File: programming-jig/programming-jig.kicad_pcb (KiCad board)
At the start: 2 copper layers, 52 x 29 mm, 9 parts, among them J1 854-22-005-10-001101, J2 854-22-005-10-001101, J3 825-22-002-10-001101, J4 CONN_02X05, J5 USB_C_Receptacle

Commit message: Use power symbols in programming jig schematic
The power lines had been drawn as regular wires with net labels.  That's
not great, so I changed them to use power symbols.  It's better now!
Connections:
- net /GND renamed GND
- net /VBUS renamed VBUS
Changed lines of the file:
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@@
   (net 23 "Net-(J5-PadA8)")
   (net 24 "Net-(J5-PadA11)")
-  (net 25 /VBUS)
-  (net 26 /GND)
-  (net 27 "Net-(J5-PadB6)")
-  (net 28 "Net-(J5-PadB7)")
+  (net 25 "Net-(J5-PadB6)")
+  (net 26 "Net-(J5-PadB7)")
+  (net 27 VBUS)
+  (net 28 GND)
   (net_class Default "This is the default net class."
     (clearance 0.2)
@@
     (uvia_dia 0.3)
     (uvia_drill 0.1)
-    (add_net /GND)
-    (add_net /VBUS)
+    (add_net GND)
     (add_net "Net-(J1-Pad1)")
     (add_net "Net-(J1-Pad2)")
@@
     (add_net "Net-(J5-PadB7)")
     (add_net "Net-(J5-PadB8)")
+    (add_net VBUS)
   )
   (module pd-buddy:Pogo_Pin_Straight_1x05_Pitch1.27mm (layer F.Cu)
@@
     (fp_line (start -4.59 9.59) (end -4.59 -0.91) (layer F.Fab) (width 0.12))
     (pad B6 thru_hole circle (at 0.4 0.65 270) (size 0.65 0.65) (drill 0.4) (layers *.Cu *.Mask)
-      (net 27 "Net-(J5-PadB6)"))
+      (net 25 "Net-(J5-PadB6)"))
     (pad B7 thru_hole circle (at -0.4 0.65 270) (size 0.65 0.65) (drill 0.4) (layers *.Cu *.Mask)
-      (net 28 "Net-(J5-PadB7)"))
+      (net 26 "Net-(J5-PadB7)"))
     (pad S1 thru_hole circle (at -4.13 1.25 270) (size 1.4 1.4) (drill 1.1) (layers *.Cu *.Mask)
-      (net 26 /GND))
+      (net 28 GND))
     (pad B9 thru_hole circle (at -1.2 0.65 270) (size 0.65 0.65) (drill 0.4) (layers *.Cu *.Mask)
-      (net 25 /VBUS))
+      (net 27 VBUS))
     (pad B4 thru_hole circle (at 1.2 0.65 270) (size 0.65 0.65) (drill 0.4) (layers *.Cu *.Mask)
-      (net 25 /VBUS))
+      (net 27 VBUS))
     (pad B12 thru_hole circle (at -2.8 0.65 270) (size 0.65 0.65) (drill 0.4) (layers *.Cu *.Mask)
-      (net 26 /GND))
+      (net 28 GND))
     (pad B5 thru_hole circle (at 0.8 1.35 270) (size 0.65 0.65) (drill 0.4) (layers *.Cu *.Mask)
       (net 13 "Net-(J5-PadB5)"))
@@
       (net 18 "Net-(J5-PadB11)"))
     (pad A1 smd rect (at -2.75 -0.66 270) (size 0.3 0.7) (layers F.Cu F.Paste F.Mask)
-      (net 26 /GND))
+      (net 28 GND))
     (pad A2 smd rect (at -2.25 -0.66 270) (size 0.3 0.7) (layers F.Cu F.Paste F.Mask)
       (net 19 "Net-(J5-PadA2)"))
@@
       (net 20 "Net-(J5-PadA3)"))
     (pad A4 smd rect (at -1.25 -0.66 270) (size 0.3 0.7) (layers F.Cu F.Paste F.Mask)
-      (net 25 /VBUS))
+      (net 27 VBUS))
     (pad A5 smd rect (at -0.75 -0.66 270) (size 0.3 0.7) (layers F.Cu F.Paste F.Mask)
       (net 21 "Net-(J5-PadA5)"))
@@
       (net 12 "Net-(J5-PadA7)"))
     (pad A12 smd rect (at 2.75 -0.66 270) (size 0.3 0.7) (layers F.Cu F.Paste F.Mask)
-      (net 26 /GND))
+      (net 28 GND))
     (pad A10 smd rect (at 1.75 -0.66 270) (size 0.3 0.7) (layers F.Cu F.Paste F.Mask)
       (net 22 "Net-(J5-PadA10)"))
     (pad A9 smd rect (at 1.25 -0.66 270) (size 0.3 0.7) (layers F.Cu F.Paste F.Mask)
-      (net 25 /VBUS))
+      (net 27 VBUS))
     (pad A8 smd rect (at 0.75 -0.66 270) (size 0.3 0.7) (layers F.Cu F.Paste F.Mask)
       (net 23 "Net-(J5-PadA8)"))
@@
       (net 24 "Net-(J5-PadA11)"))
     (pad B1 thru_hole circle (at 2.8 0.65 270) (size 0.65 0.65) (drill 0.4) (layers *.Cu *.Mask)
-      (net 26 /GND))
+      (net 28 GND))
     (pad S1 thru_hole circle (at 4.13 1.25 270) (size 1.4 1.4) (drill 1.1) (layers *.Cu *.Mask)
-      (net 26 /GND))
+      (net 28 GND))
     (pad S1 thru_hole circle (at 4.49 7.2 270) (size 1.4 1.4) (drill 1.1) (layers *.Cu *.Mask)
-      (net 26 /GND))
+      (net 28 GND))
     (pad S1 thru_hole circle (at -4.49 7.2 270) (size 1.4 1.4) (drill 1.1) (layers *.Cu *.Mask)
-      (net 26 /GND))
+      (net 28 GND))
     (pad "" np_thru_hole circle (at 3.6 0 270) (size 0.95 0.95) (drill 0.95) (layers *.Cu *.Mask))
     (pad "" np_thru_hole circle (at -3.6 0 270) (size 0.65 0.65) (drill 0.65) (layers *.Cu *.Mask))
@@
       (net 13 "Net-(J5-PadB5)"))
     (pad 2 smd rect (at 0.95 0 90) (size 0.7 1.3) (layers F.Cu F.Paste F.Mask)
-      (net 26 /GND))
+      (net 28 GND))
     (model ${KISYS3DMOD}/Resistors_SMD.3dshapes/R_0805.wrl
       (at (xyz 0 0 0))
@@
       (net 21 "Net-(J5-PadA5)"))
     (pad 2 smd rect (at 0.95 0 90) (size 0.7 1.3) (layers F.Cu F.Paste F.Mask)
-      (net 26 /GND))
+      (net 28 GND))
     (model ${KISYS3DMOD}/Resistors_SMD.3dshapes/R_0805.wrl
       (at (xyz 0 0 0))
@@
     )
     (pad 1 thru_hole rect (at 0 0 90) (size 1.7 1.7) (drill 0.762) (layers *.Cu *.Mask)
-      (net 25 /VBUS))
+      (net 27 VBUS))
     (pad 2 thru_hole oval (at 0 2.54 90) (size 1.7 1.7) (drill 0.762) (layers *.Cu *.Mask)
-      (net 26 /GND))
+      (net 28 GND))
     (model ${KISYS3DMOD}/Pin_Headers.3dshapes/Pin_Header_Straight_1x02_Pitch2.54mm.wrl
       (at (xyz 0 -0.05 0))
@@
   (segment (start 94.25 112.5) (end 94.25 111.7) (width 0.25) (layer F.Cu) (net 21))
   (via (at 94.25 112.5) (size 0.6) (drill 0.4) (layers F.Cu B.Cu) (net 21))
-  (segment (start 92.25 109.8) (end 92.25 109) (width 0.25) (layer F.Cu) (net 26))
-  (via (at 92.25 109) (size 0.6) (drill 0.4) (layers F.Cu B.Cu) (net 26))
-  (segment (start 94.25 109.8) (end 94.25 109) (width 0.25) (layer F.Cu) (net 26))
-  (via (at 94.25 109) (size 0.6) (drill 0.4) (layers F.Cu B.Cu) (net 26))
-  (segment (start 96.91 122.5) (end 95.65 122.5) (width 0.25) (layer F.Cu) (net 26))
-  (segment (start 95.65 122.5) (end 95.6 122.55) (width 0.25) (layer F.Cu) (net 26))
-  (segment (start 96.91 117) (end 95.65 117) (width 0.25) (layer F.Cu) (net 26))
-  (segment (start 95.65 117) (end 95.6 116.95) (width 0.25) (layer F.Cu) (net 26))
-  (zone (net 26) (net_name /GND) (layer B.Cu) (hatch edge 0.508)
+  (segment (start 92.25 109.8) (end 92.25 109) (width 0.25) (layer F.Cu) (net 28))
+  (via (at 92.25 109) (size 0.6) (drill 0.4) (layers F.Cu B.Cu) (net 28))
+  (segment (start 94.25 109.8) (end 94.25 109) (width 0.25) (layer F.Cu) (net 28))
+  (via (at 94.25 109) (size 0.6) (drill 0.4) (layers F.Cu B.Cu) (net 28))
+  (segment (start 96.91 122.5) (end 95.65 122.5) (width 0.25) (layer F.Cu) (net 28))
+  (segment (start 95.65 122.5) (end 95.6 122.55) (width 0.25) (layer F.Cu) (net 28))
+  (segment (start 96.91 117) (end 95.65 117) (width 0.25) (layer F.Cu) (net 28))
+  (segment (start 95.65 117) (end 95.6 116.95) (width 0.25) (layer F.Cu) (net 28))
+  (zone (net 28) (net_name GND) (layer B.Cu) (hatch edge 0.508)
     (priority 1)
     (connect_pads (clearance 0.2))
@@
     )
   )
-  (zone (net 25) (net_name /VBUS) (layer F.Cu) (hatch edge 0.508)
+  (zone (net 27) (net_name VBUS) (layer F.Cu) (hatch edge 0.508)
     (priority 1)
     (connect_pads yes (clearance 0.2))

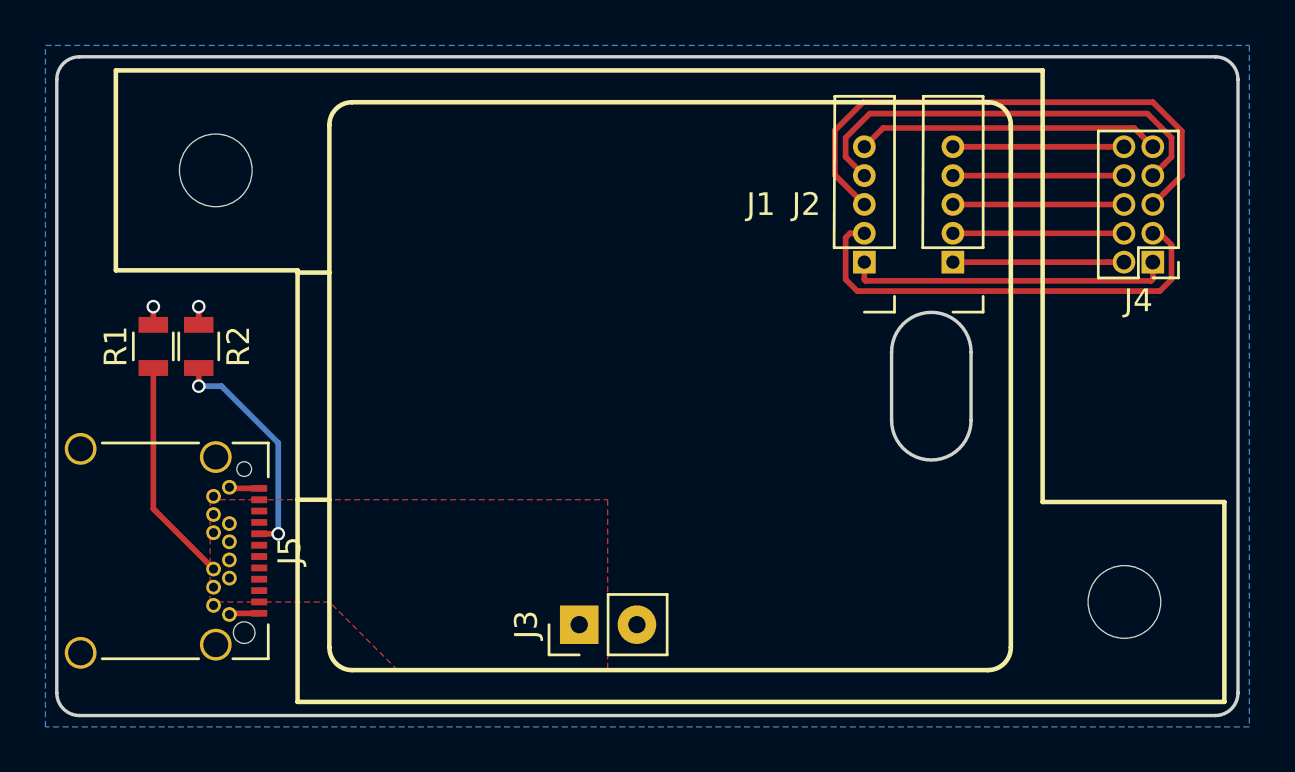
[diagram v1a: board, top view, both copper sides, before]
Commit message: Shrunk programming jig outline
By removing clearance around the printed piece, I was able to shrink the
board to 95.6% of the area it had before.  That'll save me a few cents.
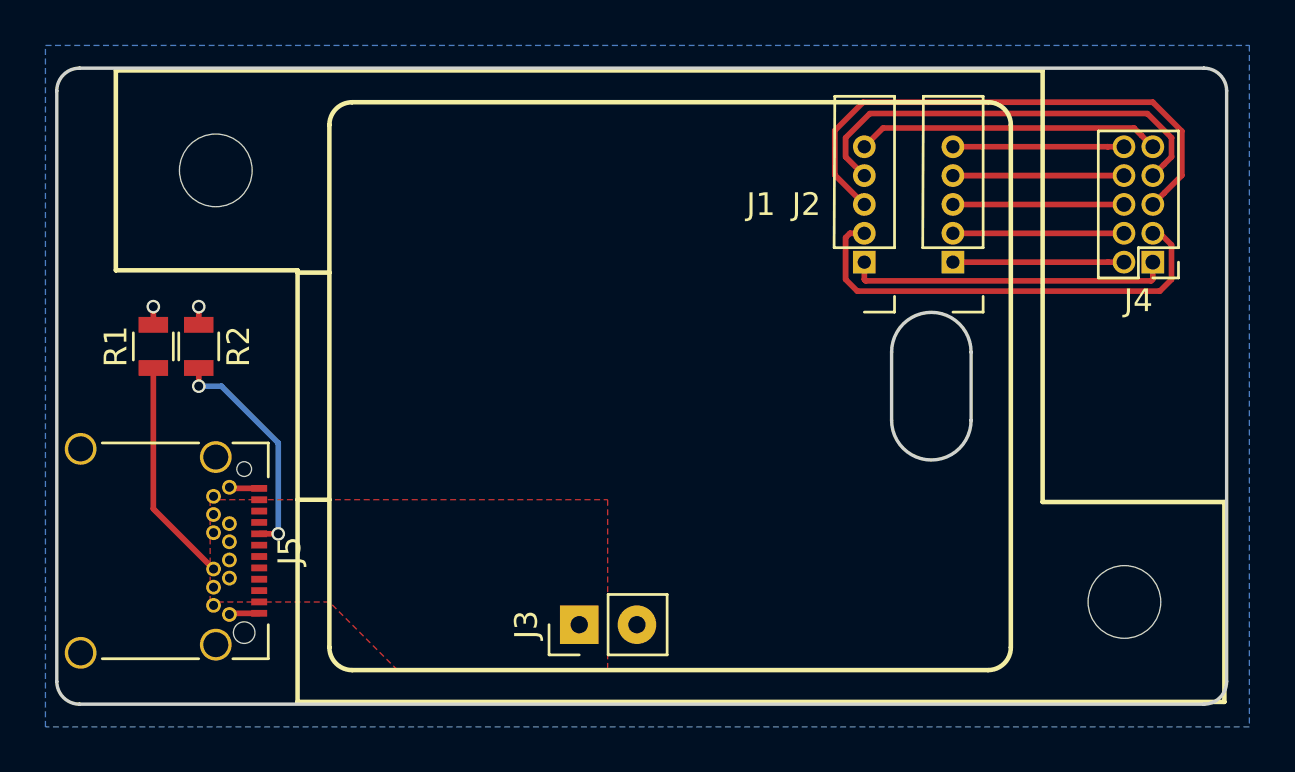
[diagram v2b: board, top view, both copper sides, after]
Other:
- board size 52 x 29 mm -> 51.5 x 28 mm
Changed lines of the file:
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@@
     (links 26)
     (no_connects 0)
-    (area 84.775 97.065 140.648334 133.295238)
+    (area 87.924999 98.424999 139.575001 126.575001)
     (thickness 1.6)
     (drawings 31)
@@
   (gr_arc (start 129 124) (end 130 124) (angle 90) (layer F.SilkS) (width 0.2))
   (gr_arc (start 129 101) (end 129 100) (angle 90) (layer F.SilkS) (width 0.2))
-  (gr_arc (start 139 99) (end 139 98) (angle 90) (layer Edge.Cuts) (width 0.15))
-  (gr_arc (start 89 99) (end 88 99) (angle 90) (layer Edge.Cuts) (width 0.15))
-  (gr_arc (start 89 126) (end 89 127) (angle 90) (layer Edge.Cuts) (width 0.15))
-  (gr_arc (start 139 126) (end 140 126) (angle 90) (layer Edge.Cuts) (width 0.15))
+  (gr_arc (start 138.5 99.5) (end 138.5 98.5) (angle 90) (layer Edge.Cuts) (width 0.15))
+  (gr_arc (start 89 99.5) (end 88 99.5) (angle 90) (layer Edge.Cuts) (width 0.15))
+  (gr_arc (start 89 125.5) (end 89 126.5) (angle 90) (layer Edge.Cuts) (width 0.15))
+  (gr_arc (start 138.5 125.5) (end 139.5 125.5) (angle 90) (layer Edge.Cuts) (width 0.15))
   (gr_line (start 100 117.5) (end 98.6 117.5) (layer F.SilkS) (width 0.2))
   (gr_line (start 98.6 107.5) (end 100 107.5) (layer F.SilkS) (width 0.2))
-  (gr_line (start 88 126) (end 88 99) (layer Edge.Cuts) (width 0.15))
-  (gr_line (start 139 127) (end 89 127) (layer Edge.Cuts) (width 0.15))
-  (gr_line (start 140 99) (end 140 126) (layer Edge.Cuts) (width 0.15))
-  (gr_line (start 89 98) (end 139 98) (layer Edge.Cuts) (width 0.15))
+  (gr_line (start 88 125.5) (end 88 99.5) (layer Edge.Cuts) (width 0.15))
+  (gr_line (start 138.5 126.5) (end 89 126.5) (layer Edge.Cuts) (width 0.15))
+  (gr_line (start 139.5 99.5) (end 139.5 125.5) (layer Edge.Cuts) (width 0.15))
+  (gr_line (start 89 98.5) (end 138.5 98.5) (layer Edge.Cuts) (width 0.15))
   (gr_line (start 90.6 98.6) (end 131.4 98.6) (layer F.SilkS) (width 0.2))
   (gr_line (start 90.6 107.4) (end 90.6 98.6) (layer F.SilkS) (width 0.2))

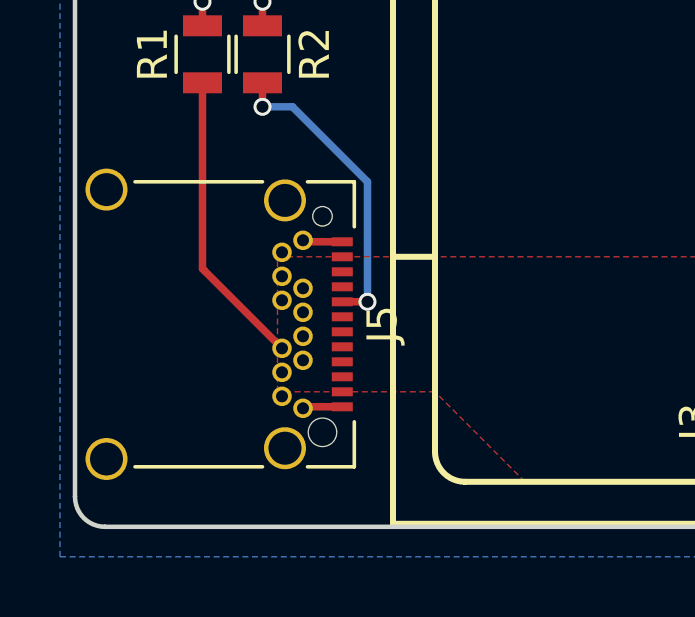
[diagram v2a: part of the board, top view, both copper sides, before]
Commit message: Use USB connector footprints from KiCad library
No need to provide our own anymore now that they're all merged upstream.
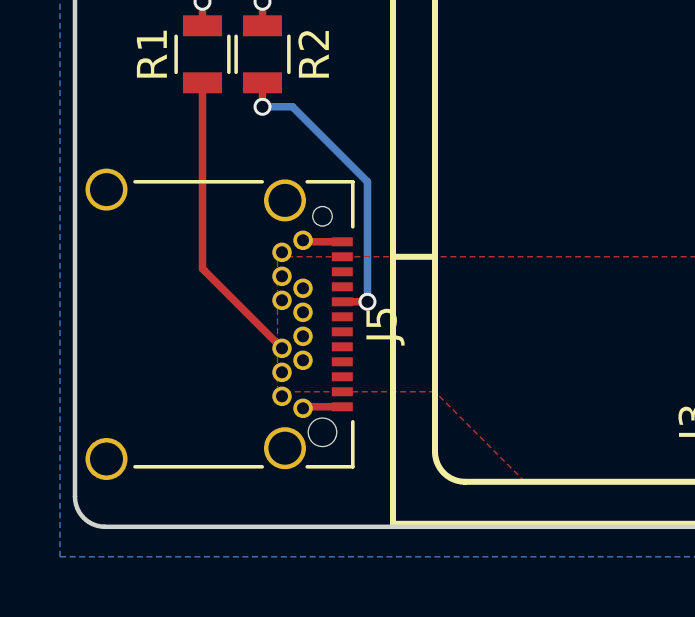
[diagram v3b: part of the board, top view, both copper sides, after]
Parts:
- J5: footprint pd-buddy:Amphenol-12401548E4#2A -> Connectors_USB:USB_C_Receptacle_Amphenol_12401548E4-2A_CircularHoles
- moved J5 4.36 mm to (91.9, 119.8)
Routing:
- net GND: track 4.26 -> 1.60 mm
- net (no net): track 0.00 -> 2.66 mm
